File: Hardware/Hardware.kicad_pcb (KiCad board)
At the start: 2 copper layers, 60 x 40 mm, 67 parts, among them J1 SWD, J2 USART2, J6 AudioJack3_SwitchT, Q1 Q_NPN_BEC BSR17A, Q2 BC547, Q3 BC547, SW1 Power_Hard, SW2 Power_Soft, SW3 Reset, U1 Opamp_Quad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

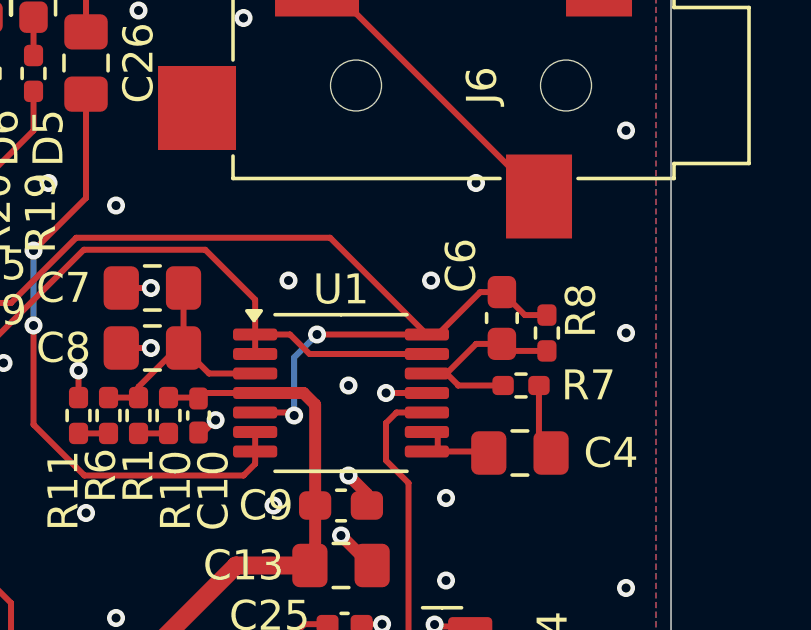
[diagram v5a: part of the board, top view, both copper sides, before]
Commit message: Inverting opamp is now also fixed on the PCB
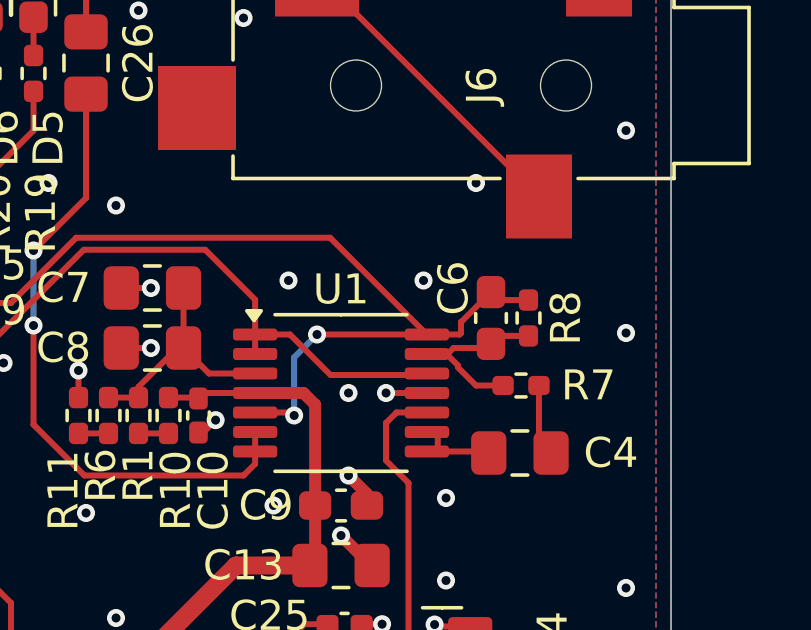
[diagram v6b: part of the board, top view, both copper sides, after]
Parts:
- moved R8 0.79 mm to (75.2, 33.8)
- moved C6 0.36 mm to (74.0, 33.8)
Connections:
- C6 pad 1: Net-(U1D-+) -> Net-(U1D--)
- R7 pad 2: Net-(U1D-+) -> Net-(U1D--)
- R8 pad 1: Net-(U1D-+) -> Net-(U1D--)
- U1 pad 12: Net-(U1D-+) -> /MCU/PA5 A5
- U1 pad 13: /MCU/PA5 A5 -> Net-(U1D--)
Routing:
- net Net-(U1D--): track 0.00 -> 6.65 mm
- net Net-(U1D-+): track 6.57 -> 0.00 mm
